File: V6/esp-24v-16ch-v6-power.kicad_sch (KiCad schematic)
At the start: 38 parts, among them J6 VIN, J7 USB_C_Receptacle_USB2.0, Q1 WPM2015-3/TR, Q2 MMUN2211LT3G, U1 SY8089A1AAC, U2 TX4138

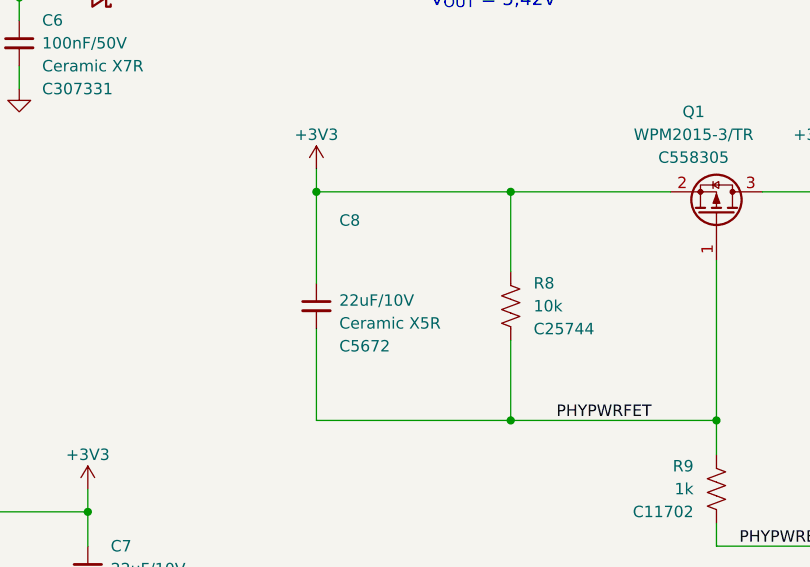
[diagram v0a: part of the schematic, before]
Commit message: addressing the PHY power rails
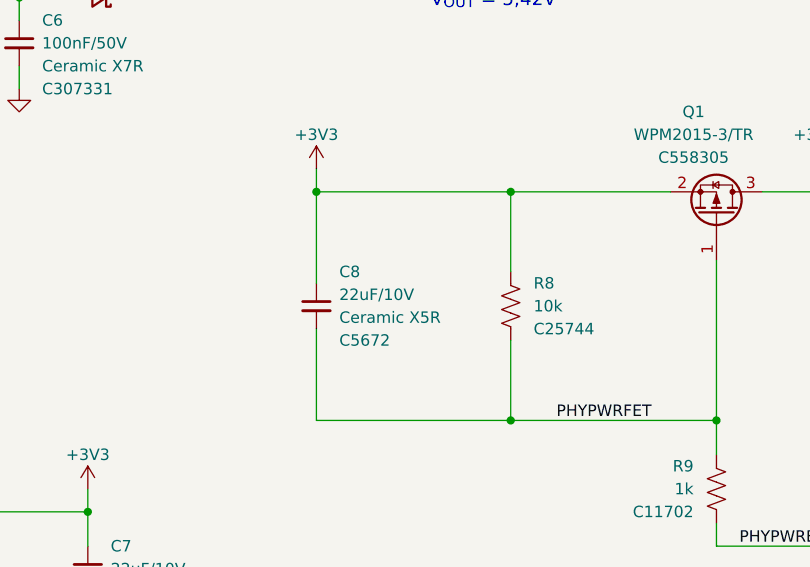
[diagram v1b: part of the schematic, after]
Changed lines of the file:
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@@
 		(dnp no)
 		(property "Reference" "C8"
-			(at 168.91 99.7013 0)
+			(at 168.91 105.41 0)
 			(show_name no)
 			(do_not_autoplace no)
@@
 		)
 		(property "Value" "22uF/10V"
-			(at 168.91 108.5913 0)
+			(at 168.91 107.95 0)
 			(show_name no)
 			(do_not_autoplace no)
@@
 		)
 		(property "Technology" "Ceramic X5R"
-			(at 168.91 111.1313 0)
+			(at 168.91 110.49 0)
 			(show_name no)
 			(do_not_autoplace no)
@@
 		)
 		(property "LCSC Part #" "C5672"
-			(at 168.91 113.6713 0)
+			(at 168.91 113.03 0)
 			(show_name no)
 			(do_not_autoplace no)

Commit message: Revising power rails
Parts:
- added C12: 100nF/50V, Tales:C_0402_1005Metric, symbol Device:C_Small
- added C14: 10uF/25V, Tales:C_0805_2012Metric, symbol Device:C_Small
- added TP1: GND, TestPoint:TestPoint_Pad_D1.5mm, symbol Connector:TestPoint
- added TP2: 5V, TestPoint:TestPoint_Pad_D1.5mm, symbol Connector:TestPoint
- added TP3: 3V3, TestPoint:TestPoint_Pad_D1.5mm, symbol Connector:TestPoint
- added TP4: 3V3LAN, TestPoint:TestPoint_Pad_D1.5mm, symbol Connector:TestPoint
- added TP5: 3V3A, TestPoint:TestPoint_Pad_D1.5mm, symbol Connector:TestPoint
- renumbered C12 to C13
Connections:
- net +3V3: now also TP3.1
- net +3V3A: now also C14.1, TP5.1
- net +3V3LAN: now also C12.1, TP4.1
- net +5V: now also TP2.1
- net GND: now also C12.2, C14.2, TP1.1
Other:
- moved on the sheet: C13, C8, D3, D6, L3, Q2, R8, R9

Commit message: Update inductor footprints
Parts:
- L1: footprint Tales:L_3x3mm_h1.5mm -> Tales:L_3x3mm_H1.5mm
- L2: footprint Tales:L_12x12mm_h6mm -> Tales:L_12x12mm_H6mm
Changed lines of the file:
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@@
 			)
 		)
-		(property "Footprint" "Tales:L_12x12mm_h6mm"
+		(property "Footprint" "Tales:L_12x12mm_H6mm"
 			(at 200.66 39.37 0)
 			(hide yes)
@@
 			)
 		)
-		(property "Footprint" "Tales:L_3x3mm_h1.5mm"
+		(property "Footprint" "Tales:L_3x3mm_H1.5mm"
 			(at 88.9 132.08 0)
 			(hide yes)

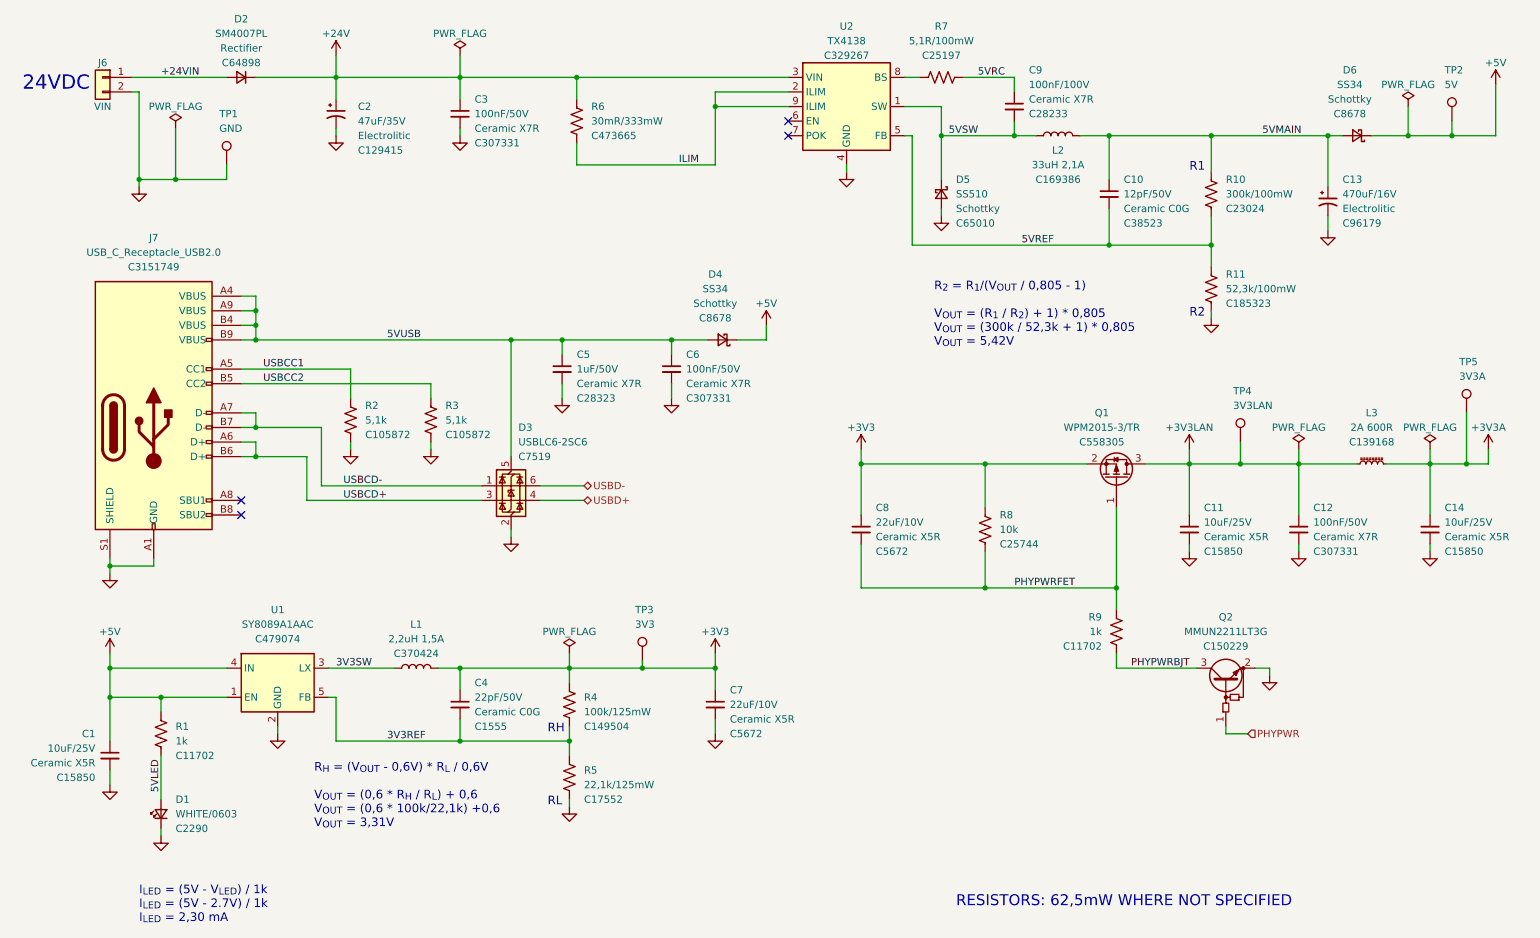
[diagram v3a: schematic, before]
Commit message: Included test points
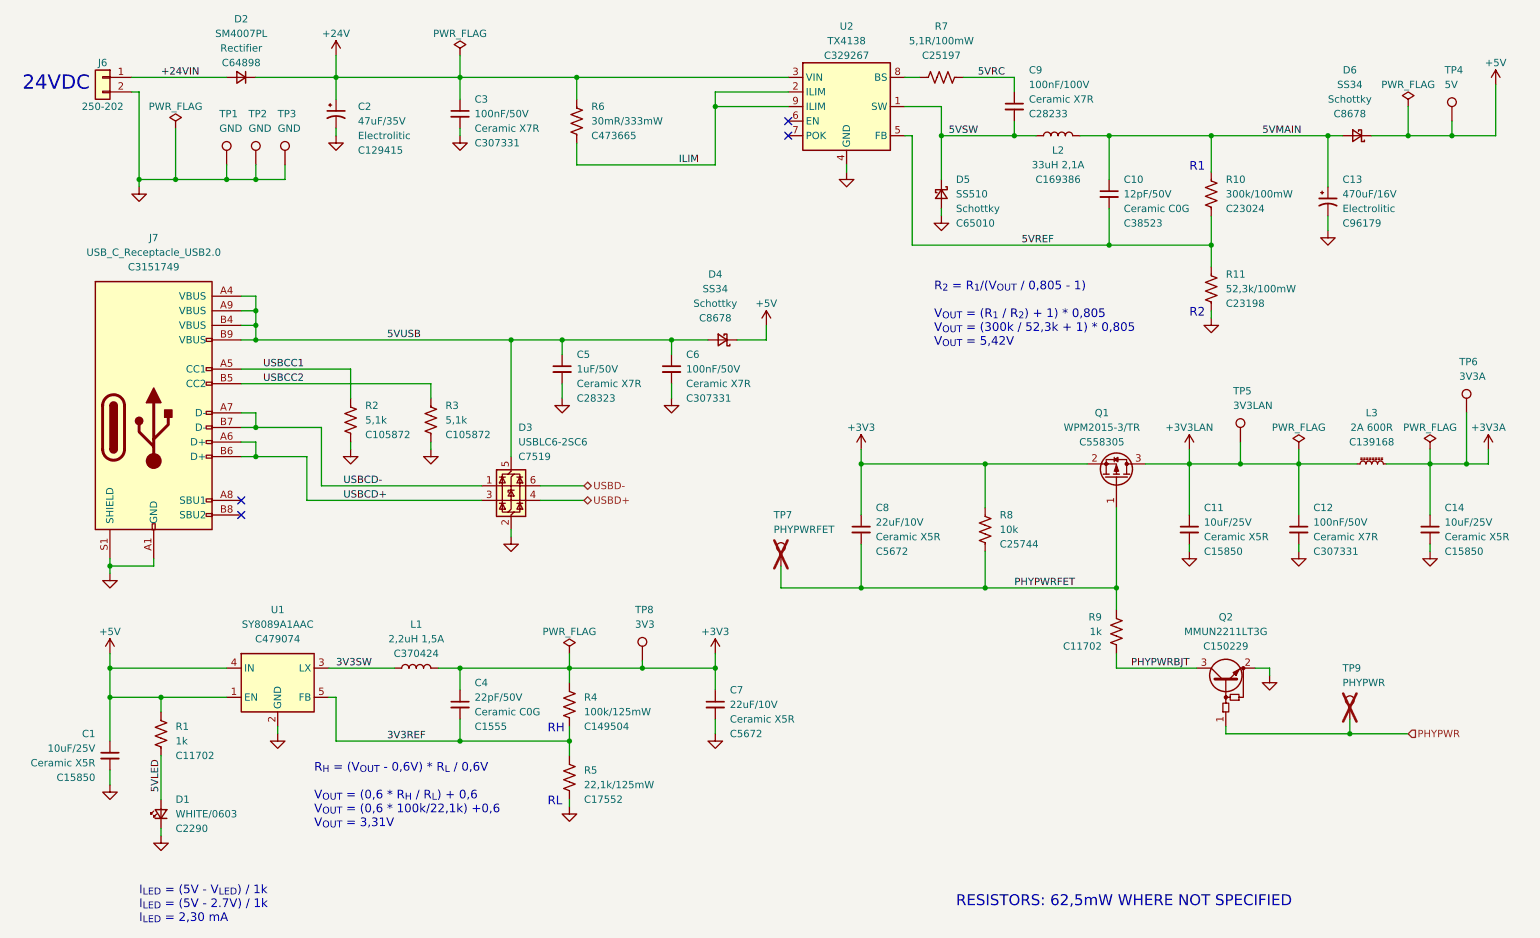
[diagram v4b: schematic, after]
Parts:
- added TP2, TP3: GND, Tales:TestPoint_Keystone_5019_Miniature, symbol Connector:TestPoint
- added TP7: PHYPWRFET, TestPoint:TestPoint_Pad_D1.5mm, symbol Connector:TestPoint
- added TP9: PHYPWR, TestPoint:TestPoint_Pad_D1.5mm, symbol Connector:TestPoint
- J6: value VIN -> 250-202
- R11: LCSC Part # C185323 -> C23198; Mfr Yageo -> Uniroyal; Mfr PN RC0603FR-0752K3L -> 0603WAF5232T5E; Vendor PN C185323 -> C23198
- TP1: footprint TestPoint:TestPoint_Pad_D1.5mm -> Tales:TestPoint_Keystone_5019_Miniature; JLCPCB BOM (none) -> 0
- TP4: renamed from TP2; footprint TestPoint:TestPoint_Pad_D1.5mm -> Tales:TestPoint_Keystone_5019_Miniature; JLCPCB BOM (none) -> 0
- TP5: renamed from TP4; JLCPCB BOM (none) -> 0
- TP6: renamed from TP5; JLCPCB BOM (none) -> 0
- TP8: renamed from TP3; footprint TestPoint:TestPoint_Pad_D1.5mm -> Tales:TestPoint_Keystone_5019_Miniature; JLCPCB BOM (none) -> 0
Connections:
- net GND: now also TP2.1, TP3.1
- net PHYPWR: now also TP9.1
- net PHYPWRFET: now also TP7.1

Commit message: Removed test points that didn't fit the PCB
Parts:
- TP7, TP9: now left out of the parts list
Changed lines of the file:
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@@
 		(body_style 1)
 		(exclude_from_sim no)
-		(in_bom yes)
-		(on_board yes)
+		(in_bom no)
+		(on_board no)
 		(in_pos_files yes)
 		(dnp yes)
@@
 		(body_style 1)
 		(exclude_from_sim no)
-		(in_bom yes)
-		(on_board yes)
+		(in_bom no)
+		(on_board no)
 		(in_pos_files yes)
 		(dnp yes)

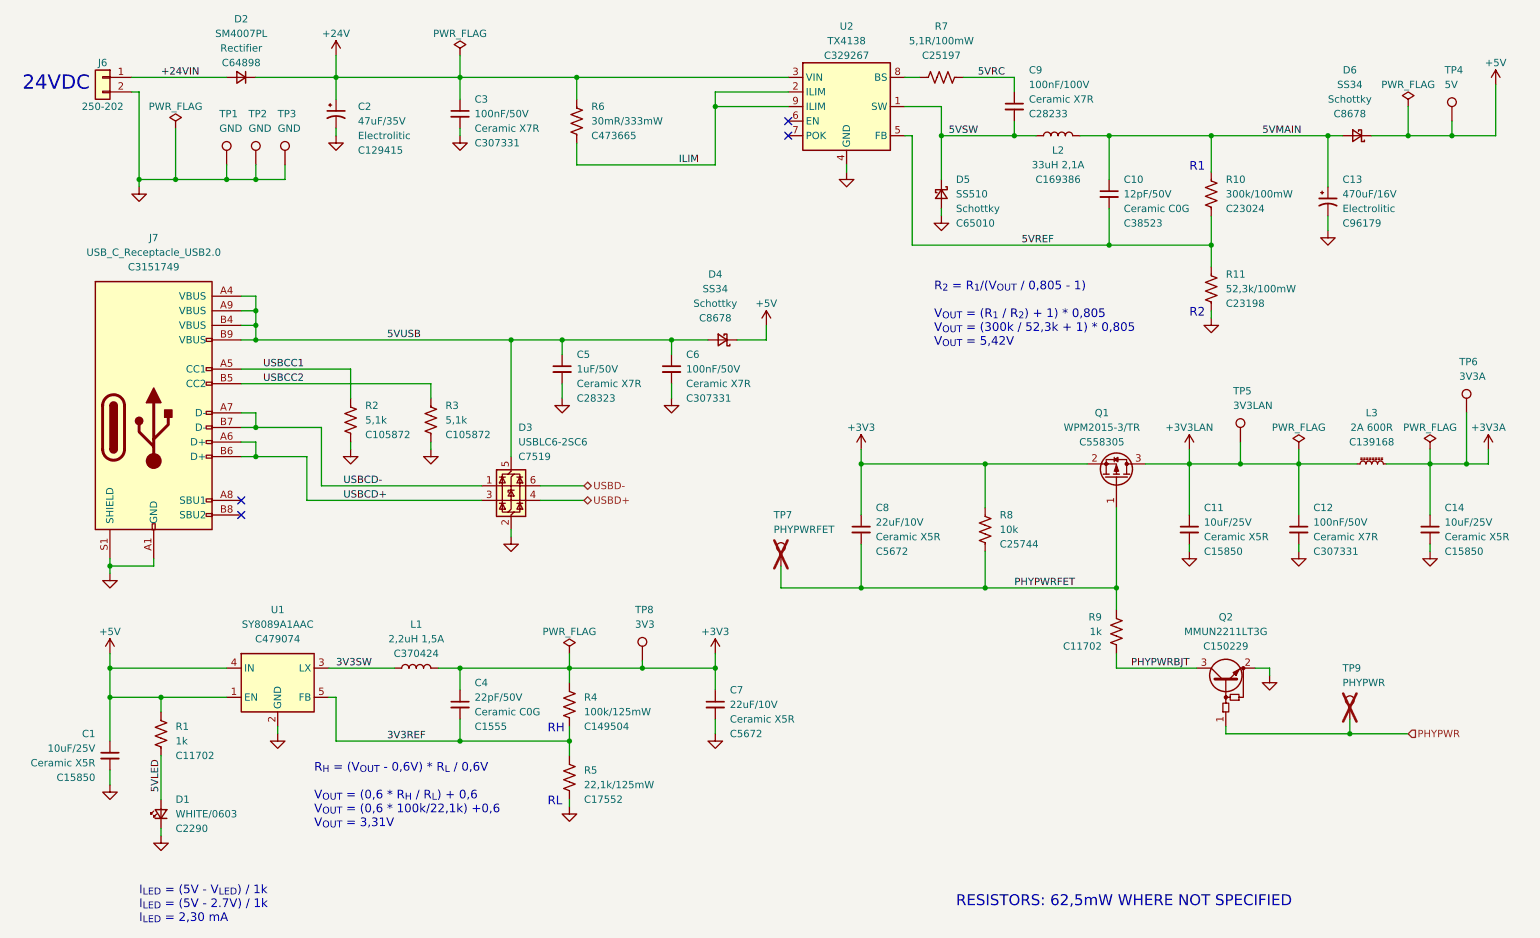
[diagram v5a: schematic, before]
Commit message: Included a shunt resistor on the 5V rail, for measuring current during development.
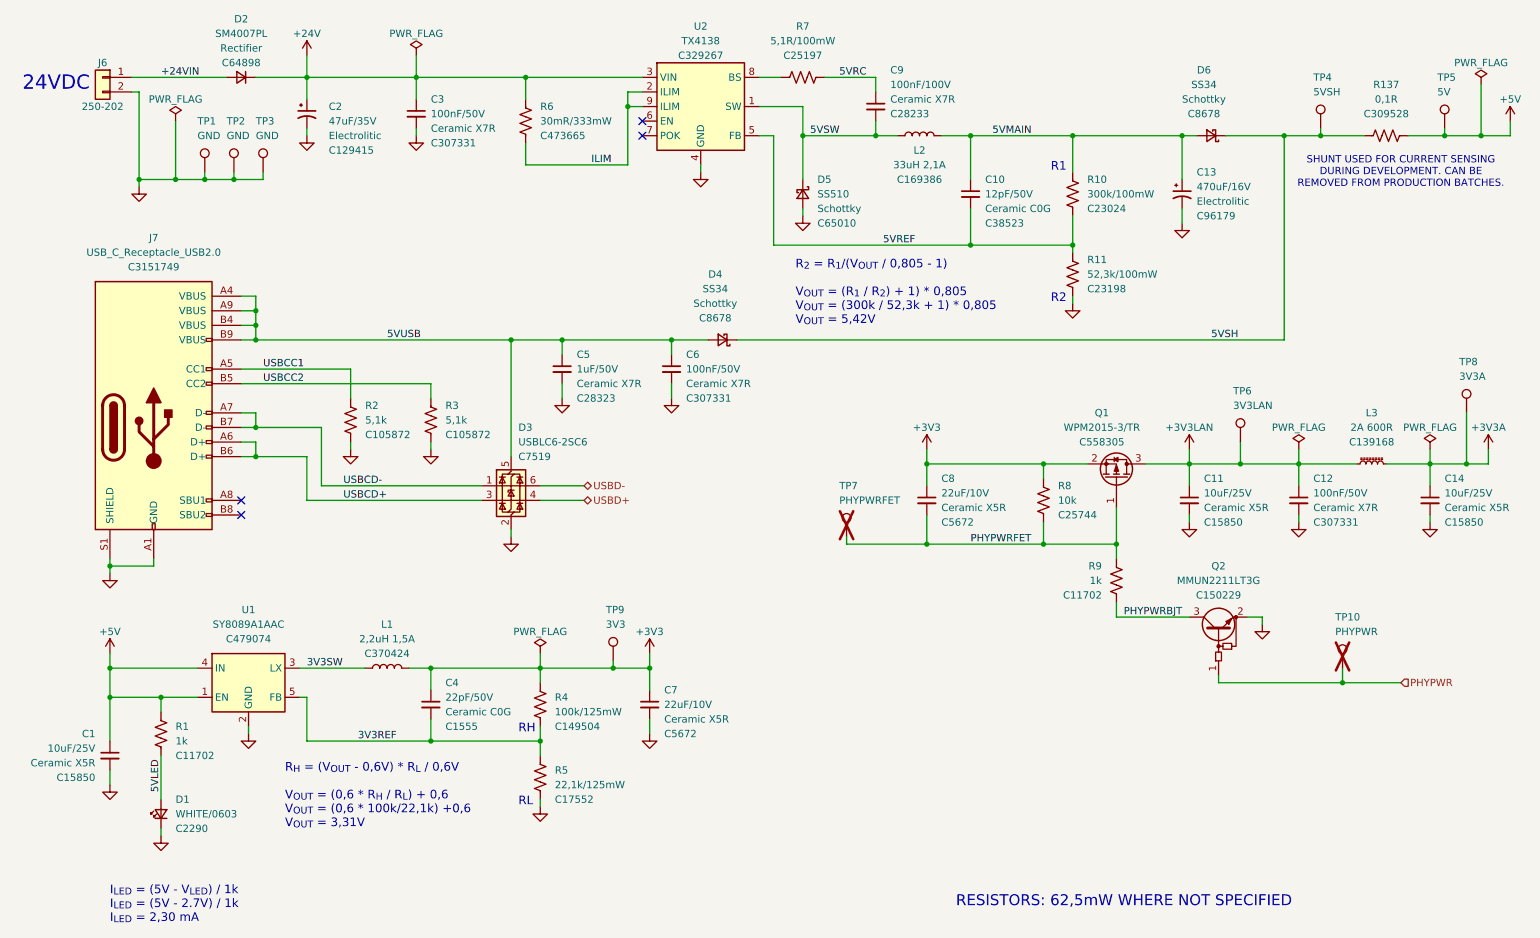
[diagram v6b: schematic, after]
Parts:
- added R137: 0,1R, Tales:C_1206_3216Metric, symbol Device:R_US
- added TP4: 5VSH, Tales:TestPoint_Keystone_5019_Miniature, symbol Connector:TestPoint
- renumbered TP9 to TP10, TP4 to TP5, TP5 to TP6, TP6 to TP8, TP8 to TP9
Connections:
- net +5V: now also R137.1; no longer D4.1 (K), D6.1 (K)
- new net 5VSH: D4.1 (K), D6.1 (K), R137.2, TP4.1
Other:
- note added: "SHUNT USED FOR CURRENT SENSING DURING DEVELOPMENT. CAN BE REMOVED FROM PRODUCTION BATCHES."
- moved on the sheet: C10, C11, C12, C13, C14, C2, C3, C4, C7, C8, C9, D5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

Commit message: Added voltage monitors for both ESP32 and LAN8710A
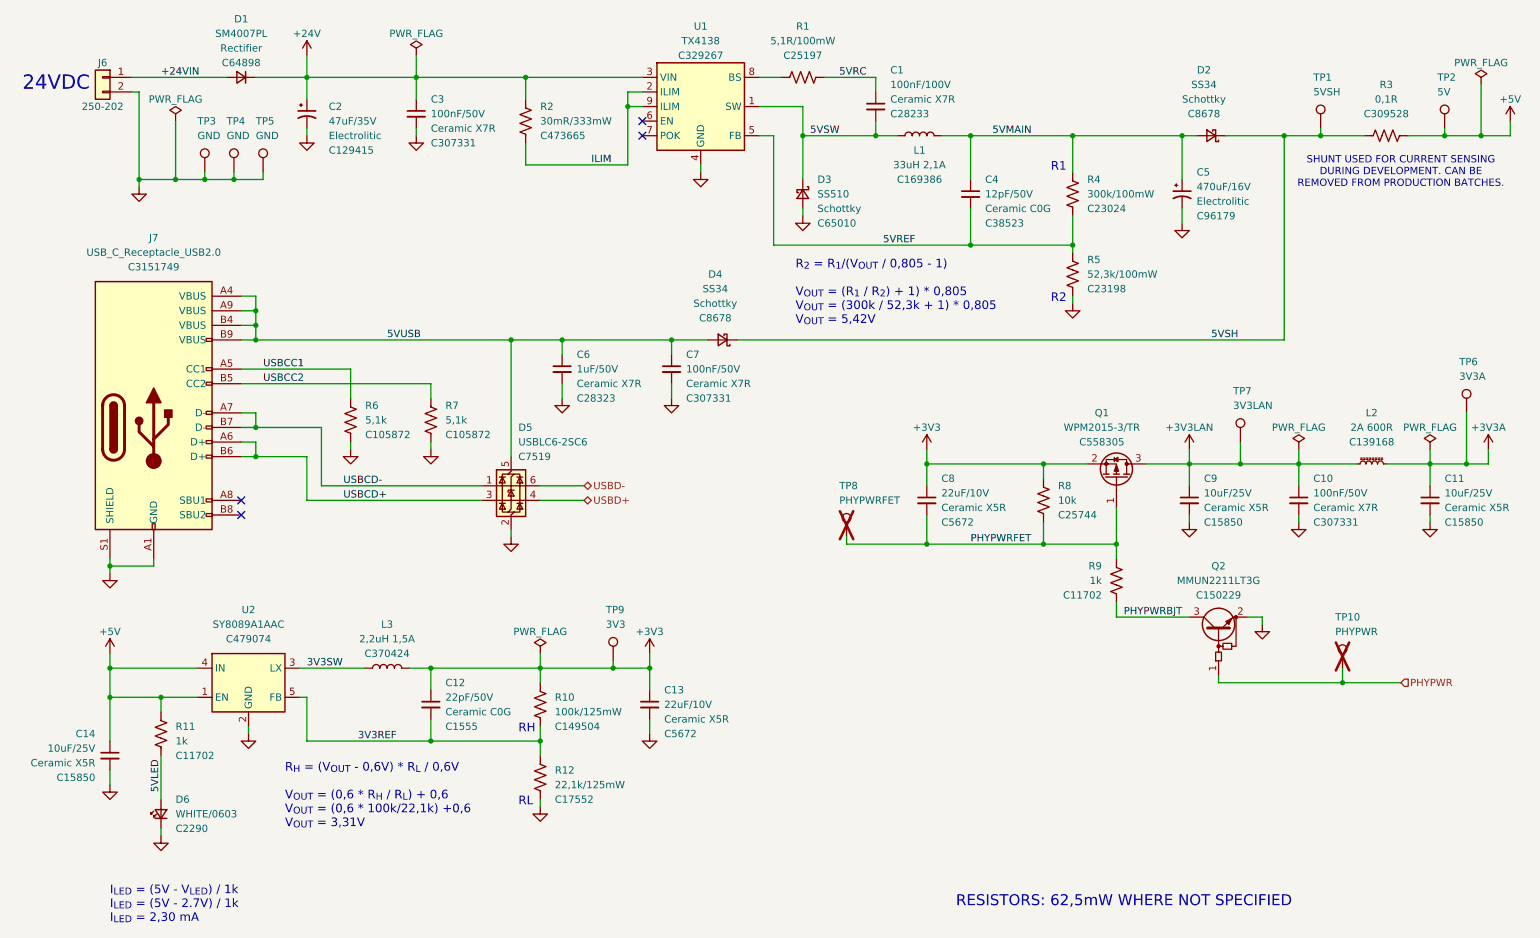
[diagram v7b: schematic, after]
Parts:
- renumbered C9 to C1, C12 to C10, C14 to C11, C4 to C12, C7 to C13, C1 to C14, C10 to C4, C13 to C5, C5 to C6, C6 to C7, C11 to C9, D2 to D1, D6 to D2, D5 to D3, D3 to D5, D1 to D6, L2 to L1, L3 to L2, L1 to L3, R7 to R1, R4 to R10, R1 to R11, R5 to R12, R6 to R2, R137 to R3, R10 to R4, R11 to R5, R2 to R6, R3 to R7, TP4 to TP1, TP5 to TP2, TP1 to TP3, TP2 to TP4, TP3 to TP5, TP8 to TP6, TP6 to TP7, TP7 to TP8, U2 to U1, U1 to U2
